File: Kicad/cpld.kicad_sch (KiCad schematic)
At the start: 16 parts, among them J2 Conn_01x06_Pin, U7 AMS1117-3.3, U9 XC95144XL-TQ144

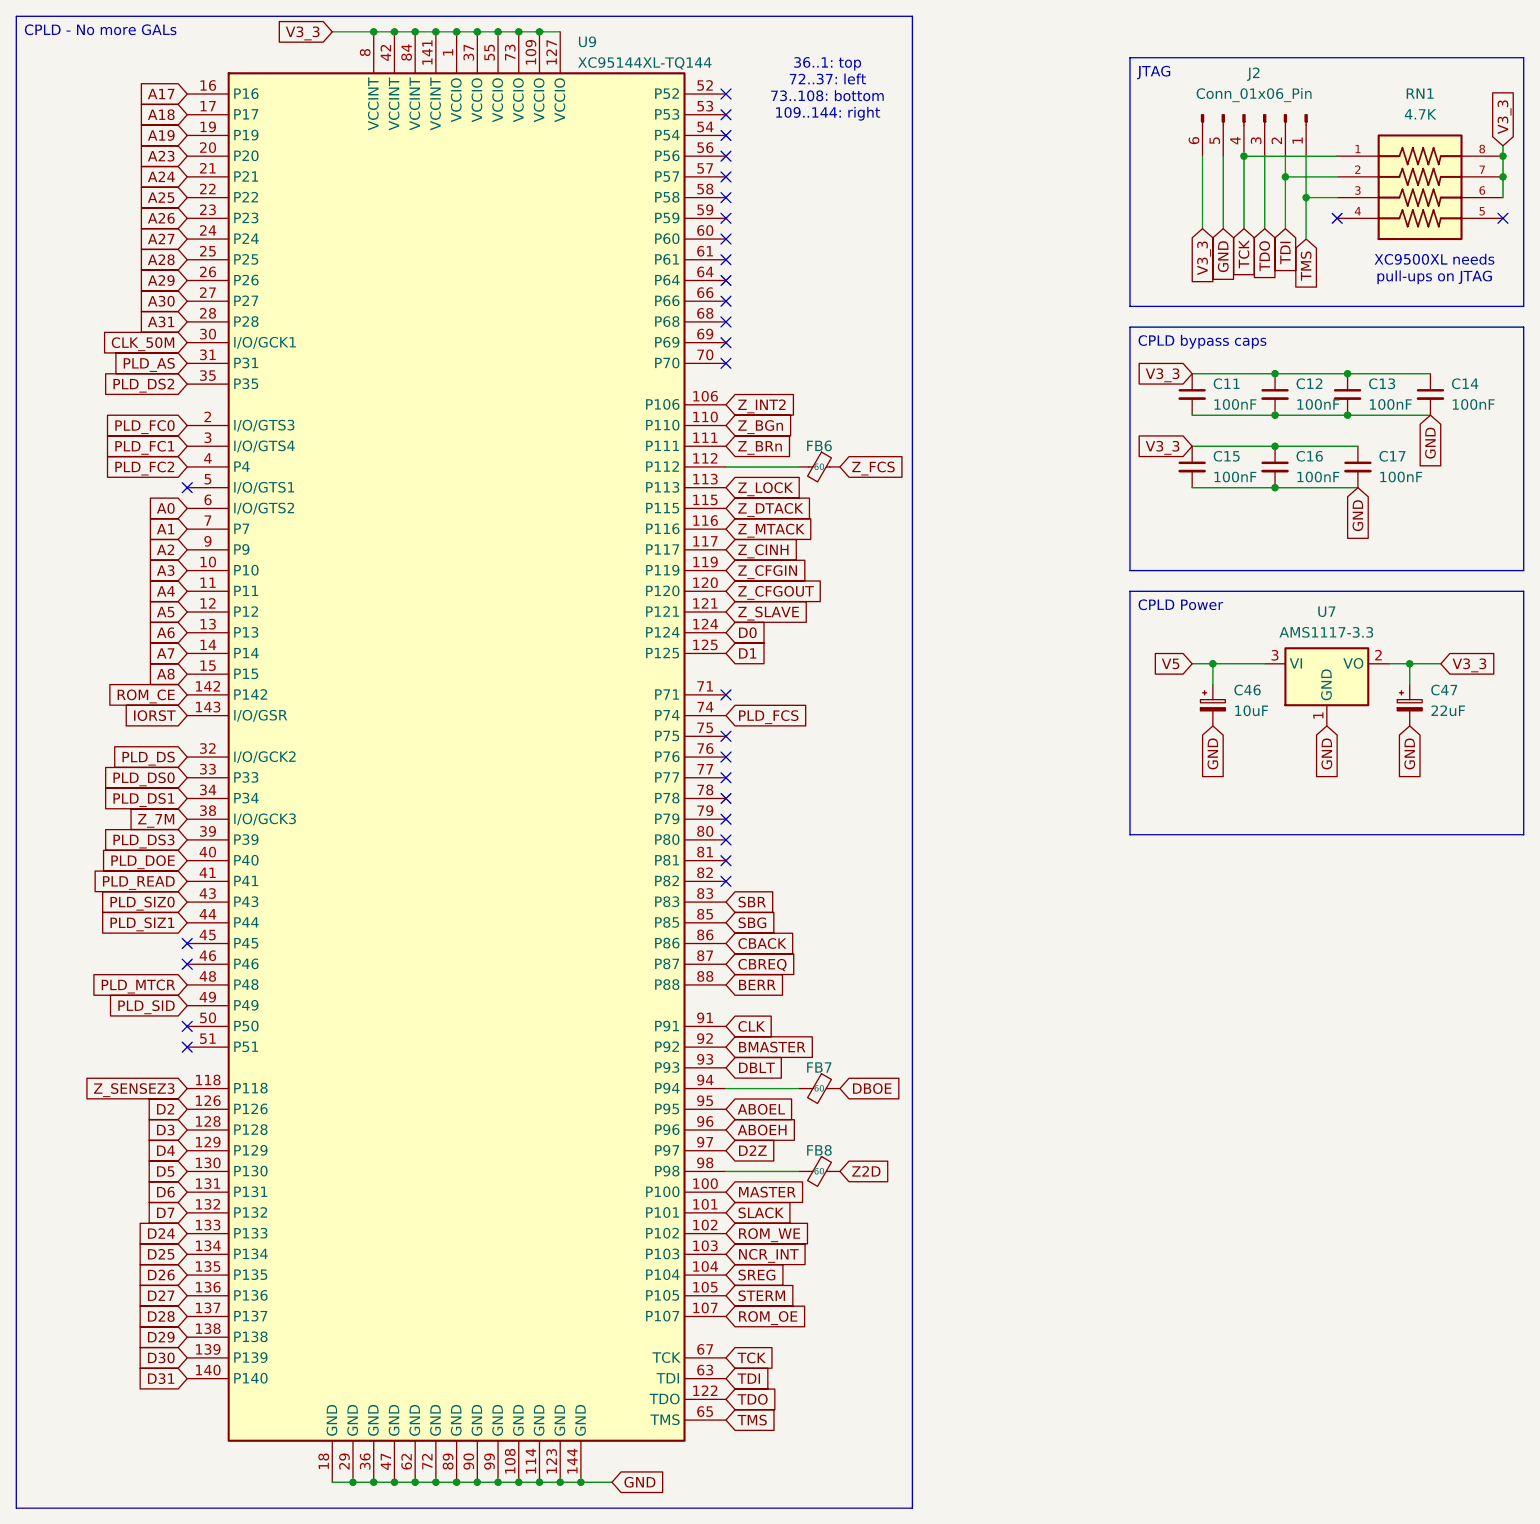
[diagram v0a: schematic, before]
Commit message: CPLD pin net swap (issue #7)
• PLD_FC0-FC2 nets move from Pin 2-4 to 75-77
• PLD_DS0-DS2 nets move from Pin 33-35 to 78-80
• ROM_WE net move from Pin 102  to 5
• ROM_OE net move from Pin 107 to 4

Additionally moved ROM_CE to P3 and PLD_DS3 to P81
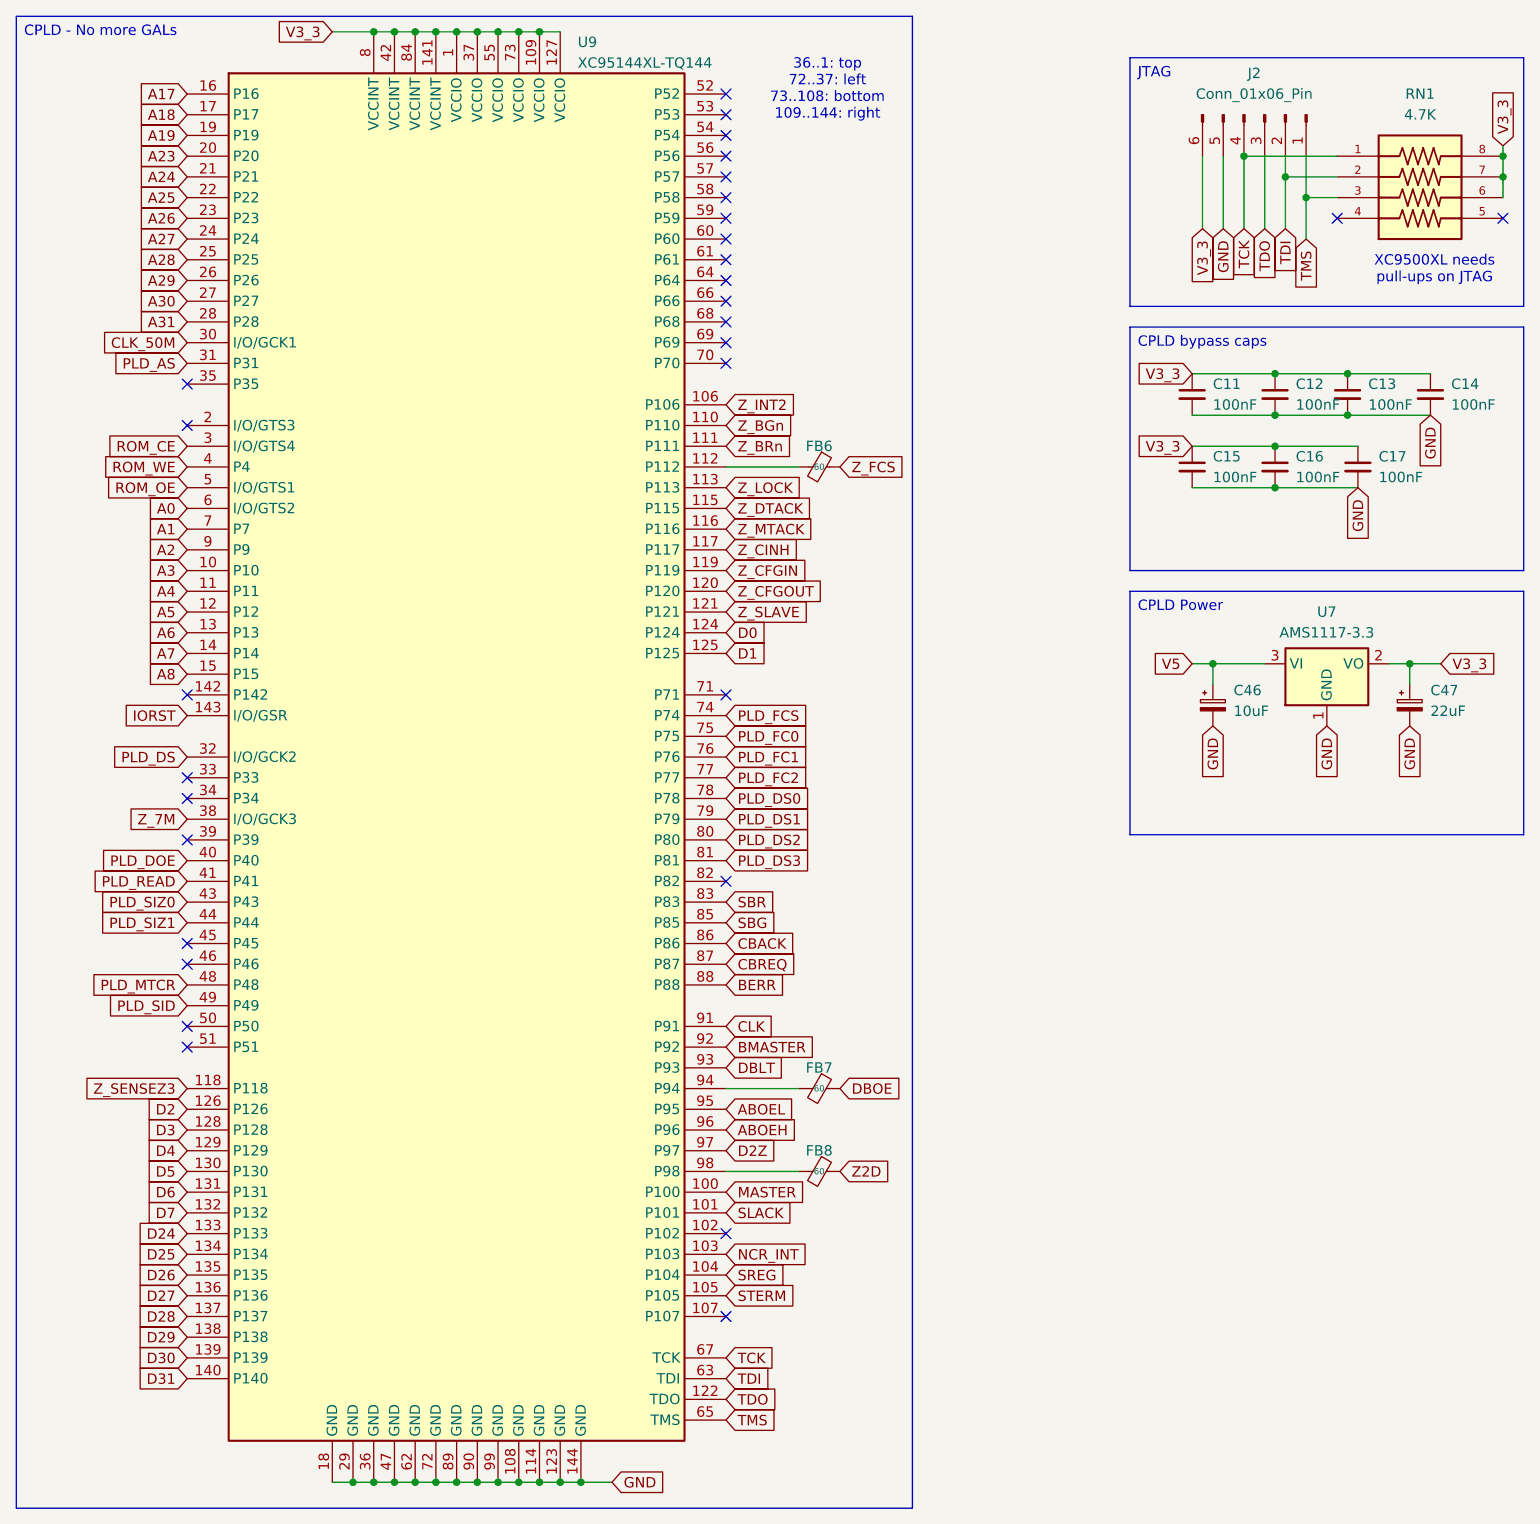
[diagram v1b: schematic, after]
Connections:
- net PLD_DS0: now also U9.78 (P78); no longer U9.33 (P33)
- net PLD_DS1: now also U9.79 (P79); no longer U9.34 (P34)
- net PLD_DS2: now also U9.80 (P80); no longer U9.35 (P35)
- net PLD_DS3: now also U9.81 (P81); no longer U9.39 (P39)
- net PLD_FC0: now also U9.75 (P75); no longer U9.2 (I/O/GTS3)
- net PLD_FC1: now also U9.76 (P76); no longer U9.3 (I/O/GTS4)
- net PLD_FC2: now also U9.77 (P77); no longer U9.4 (P4)
- net ROM_CE: now also U9.3 (I/O/GTS4); no longer U9.142 (P142)
- net ROM_OE: now also U9.5 (I/O/GTS1); no longer U9.107 (P107)
- net ROM_WE: now also U9.4 (P4); no longer U9.102 (P102)

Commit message: Update sheet, add pull down on ROM_CE
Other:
- company: (none) -> amiga.technology
- title: (none) -> A4092
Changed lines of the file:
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@@
 	(generator_version "9.0")
 	(paper "A4")
+	(title_block
+		(title "A4092")
+		(rev "PROTO0")
+		(company "amiga.technology")
+	)
 	(text "36..1: top\n72..37: left \n73..108: bottom\n109..144: right"
 		(exclude_from_sim no)

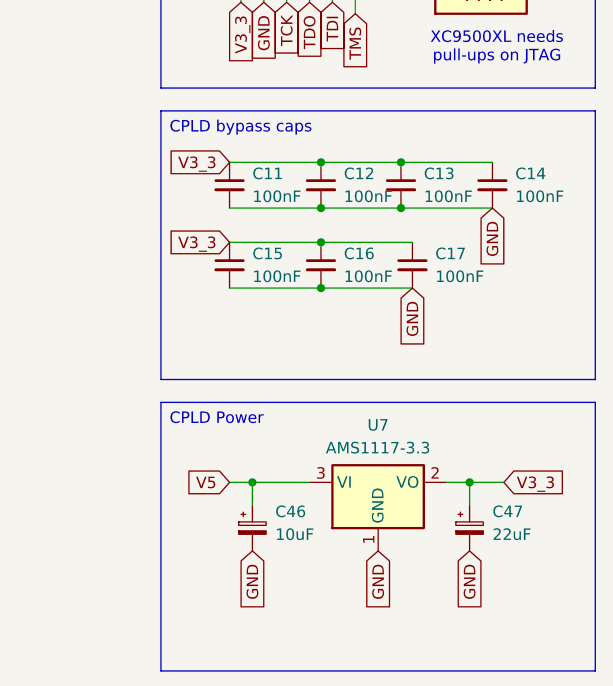
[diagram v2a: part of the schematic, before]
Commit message: Rename majority of bypass capacitors to match their Uxx
i.e. U4 will have C4A, C4B, C4C, C4D
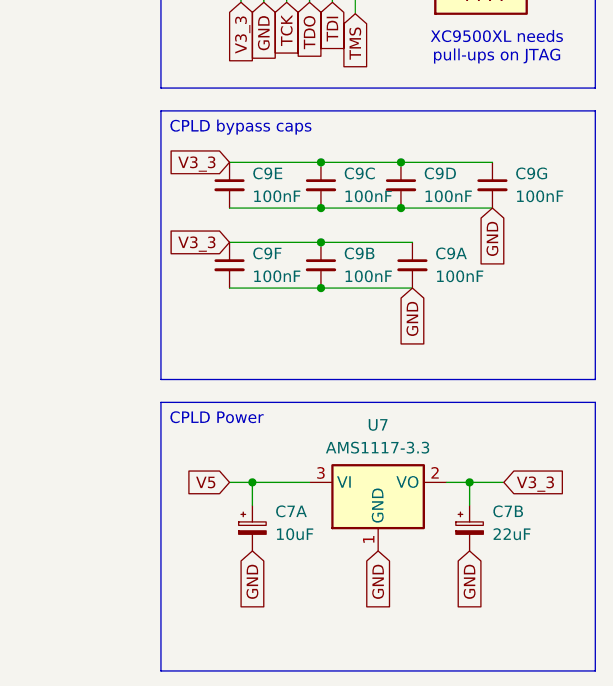
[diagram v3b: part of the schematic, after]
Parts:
- renumbered C46 to C7A, C47 to C7B, C17 to C9A, C16 to C9B, C12 to C9C, C13 to C9D, C11 to C9E, C15 to C9F, C14 to C9G
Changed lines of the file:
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@@
 		(dnp no)
 		(fields_autoplaced yes)
-		(property "Reference" "C15"
+		(property "Reference" "C9F"
 			(at 160.02 67.3162 0)
 			(effects
@@
 			(project "A4092"
 				(path "/8f9f4021-47aa-41d9-bea7-f6ccf72098bb/6ae4417c-9681-4757-b289-033d6e31deb3"
-					(reference "C15")
+					(reference "C9F")
 					(unit 1)
 				)
@@
 		(dnp no)
 		(fields_autoplaced yes)
-		(property "Reference" "C46"
+		(property "Reference" "C7A"
 			(at 162.56 95.9738 0)
 			(effects
@@
 			(project "A4092"
 				(path "/8f9f4021-47aa-41d9-bea7-f6ccf72098bb/6ae4417c-9681-4757-b289-033d6e31deb3"
-					(reference "C46")
+					(reference "C7A")
 					(unit 1)
 				)
@@
 		(dnp no)
 		(fields_autoplaced yes)
-		(property "Reference" "C17"
+		(property "Reference" "C9A"
 			(at 180.34 67.3162 0)
 			(effects
@@
 			(project "A4092"
 				(path "/8f9f4021-47aa-41d9-bea7-f6ccf72098bb/6ae4417c-9681-4757-b289-033d6e31deb3"
-					(reference "C17")
+					(reference "C9A")
 					(unit 1)
 				)
@@
 		(dnp no)
 		(fields_autoplaced yes)
-		(property "Reference" "C13"
+		(property "Reference" "C9D"
 			(at 179.07 58.4262 0)
 			(effects
@@
 			(project "A4092"
 				(path "/8f9f4021-47aa-41d9-bea7-f6ccf72098bb/6ae4417c-9681-4757-b289-033d6e31deb3"
-					(reference "C13")
+					(reference "C9D")
 					(unit 1)
 				)
@@
 		(dnp no)
 		(fields_autoplaced yes)
-		(property "Reference" "C11"
+		(property "Reference" "C9E"
 			(at 160.02 58.4262 0)
 			(effects
@@
 			(project ""
 				(path "/8f9f4021-47aa-41d9-bea7-f6ccf72098bb/6ae4417c-9681-4757-b289-033d6e31deb3"
-					(reference "C11")
+					(reference "C9E")
 					(unit 1)
 				)
@@
 		(dnp no)
 		(fields_autoplaced yes)
-		(property "Reference" "C14"
+		(property "Reference" "C9G"
 			(at 189.23 58.4262 0)
 			(effects
@@
 			(project "A4092"
 				(path "/8f9f4021-47aa-41d9-bea7-f6ccf72098bb/6ae4417c-9681-4757-b289-033d6e31deb3"
-					(reference "C14")
+					(reference "C9G")
 					(unit 1)
 				)
@@
 		(dnp no)
 		(fields_autoplaced yes)
-		(property "Reference" "C47"
+		(property "Reference" "C7B"
 			(at 186.69 95.9738 0)
 			(effects
@@
 			(project "A4092"
 				(path "/8f9f4021-47aa-41d9-bea7-f6ccf72098bb/6ae4417c-9681-4757-b289-033d6e31deb3"
-					(reference "C47")
+					(reference "C7B")
 					(unit 1)
 				)
@@
 		(dnp no)
 		(fields_autoplaced yes)
-		(property "Reference" "C12"
+		(property "Reference" "C9C"
 			(at 170.18 58.4262 0)
 			(effects
@@
 			(project ""
 				(path "/8f9f4021-47aa-41d9-bea7-f6ccf72098bb/6ae4417c-9681-4757-b289-033d6e31deb3"
-					(reference "C12")
+					(reference "C9C")
 					(unit 1)
 				)
@@
 		(dnp no)
 		(fields_autoplaced yes)
-		(property "Reference" "C16"
+		(property "Reference" "C9B"
 			(at 170.18 67.3162 0)
 			(effects
@@
 			(project "A4092"
 				(path "/8f9f4021-47aa-41d9-bea7-f6ccf72098bb/6ae4417c-9681-4757-b289-033d6e31deb3"
-					(reference "C16")
-					(unit 1)
-				)
+					(reference "C9B")
+					(unit 1)
+				)

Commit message: Revert: Rename majority of bypass capacitors to match their Uxx
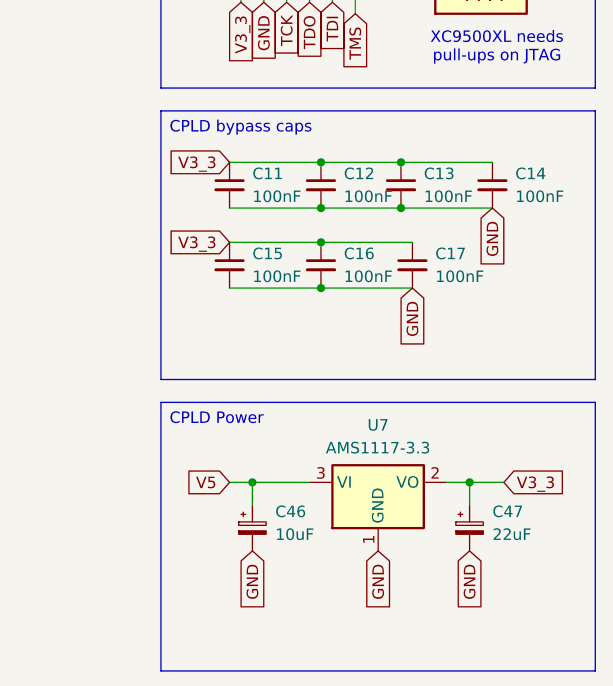
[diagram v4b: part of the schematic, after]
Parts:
- renumbered C9E to C11, C9C to C12, C9D to C13, C9G to C14, C9F to C15, C9B to C16, C9A to C17, C7A to C46, C7B to C47
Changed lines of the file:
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@@
 		(dnp no)
 		(fields_autoplaced yes)
-		(property "Reference" "C9F"
+		(property "Reference" "C15"
 			(at 160.02 67.3162 0)
 			(effects
@@
 			(project "A4092"
 				(path "/8f9f4021-47aa-41d9-bea7-f6ccf72098bb/6ae4417c-9681-4757-b289-033d6e31deb3"
-					(reference "C9F")
+					(reference "C15")
 					(unit 1)
 				)
@@
 		(dnp no)
 		(fields_autoplaced yes)
-		(property "Reference" "C7A"
+		(property "Reference" "C46"
 			(at 162.56 95.9738 0)
 			(effects
@@
 			(project "A4092"
 				(path "/8f9f4021-47aa-41d9-bea7-f6ccf72098bb/6ae4417c-9681-4757-b289-033d6e31deb3"
-					(reference "C7A")
+					(reference "C46")
 					(unit 1)
 				)
@@
 		(dnp no)
 		(fields_autoplaced yes)
-		(property "Reference" "C9A"
+		(property "Reference" "C17"
 			(at 180.34 67.3162 0)
 			(effects
@@
 			(project "A4092"
 				(path "/8f9f4021-47aa-41d9-bea7-f6ccf72098bb/6ae4417c-9681-4757-b289-033d6e31deb3"
-					(reference "C9A")
+					(reference "C17")
 					(unit 1)
 				)
@@
 		(dnp no)
 		(fields_autoplaced yes)
-		(property "Reference" "C9D"
+		(property "Reference" "C13"
 			(at 179.07 58.4262 0)
 			(effects
@@
 			(project "A4092"
 				(path "/8f9f4021-47aa-41d9-bea7-f6ccf72098bb/6ae4417c-9681-4757-b289-033d6e31deb3"
-					(reference "C9D")
+					(reference "C13")
 					(unit 1)
 				)
@@
 		(dnp no)
 		(fields_autoplaced yes)
-		(property "Reference" "C9E"
+		(property "Reference" "C11"
 			(at 160.02 58.4262 0)
 			(effects
@@
 			(project ""
 				(path "/8f9f4021-47aa-41d9-bea7-f6ccf72098bb/6ae4417c-9681-4757-b289-033d6e31deb3"
-					(reference "C9E")
+					(reference "C11")
 					(unit 1)
 				)
@@
 		(dnp no)
 		(fields_autoplaced yes)
-		(property "Reference" "C9G"
+		(property "Reference" "C14"
 			(at 189.23 58.4262 0)
 			(effects
@@
 			(project "A4092"
 				(path "/8f9f4021-47aa-41d9-bea7-f6ccf72098bb/6ae4417c-9681-4757-b289-033d6e31deb3"
-					(reference "C9G")
+					(reference "C14")
 					(unit 1)
 				)
@@
 		(dnp no)
 		(fields_autoplaced yes)
-		(property "Reference" "C7B"
+		(property "Reference" "C47"
 			(at 186.69 95.9738 0)
 			(effects
@@
 			(project "A4092"
 				(path "/8f9f4021-47aa-41d9-bea7-f6ccf72098bb/6ae4417c-9681-4757-b289-033d6e31deb3"
-					(reference "C7B")
+					(reference "C47")
 					(unit 1)
 				)
@@
 		(dnp no)
 		(fields_autoplaced yes)
-		(property "Reference" "C9C"
+		(property "Reference" "C12"
 			(at 170.18 58.4262 0)
 			(effects
@@
 			(project ""
 				(path "/8f9f4021-47aa-41d9-bea7-f6ccf72098bb/6ae4417c-9681-4757-b289-033d6e31deb3"
-					(reference "C9C")
+					(reference "C12")
 					(unit 1)
 				)
@@
 		(dnp no)
 		(fields_autoplaced yes)
-		(property "Reference" "C9B"
+		(property "Reference" "C16"
 			(at 170.18 67.3162 0)
 			(effects
@@
 			(project "A4092"
 				(path "/8f9f4021-47aa-41d9-bea7-f6ccf72098bb/6ae4417c-9681-4757-b289-033d6e31deb3"
-					(reference "C9B")
-					(unit 1)
-				)
+					(reference "C16")
+					(unit 1)
+				)

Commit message: Replace C47 and C46 with Tantalum capacitors
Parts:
- C46, C47: footprint Capacitor_SMD:CP_Elec_6.3x7.7 -> Capacitor_Tantalum_SMD:CP_EIA-3528-15_AVX-H_HandSolder
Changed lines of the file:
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@@
 			)
 		)
-		(property "Footprint" "Capacitor_SMD:CP_Elec_6.3x7.7"
+		(property "Footprint" "Capacitor_Tantalum_SMD:CP_EIA-3528-15_AVX-H_HandSolder"
 			(at 160.02 97.79 0)
 			(effects
@@
 			)
 		)
-		(property "Footprint" "Capacitor_SMD:CP_Elec_6.3x7.7"
+		(property "Footprint" "Capacitor_Tantalum_SMD:CP_EIA-3528-15_AVX-H_HandSolder"
 			(at 184.15 97.79 0)
 			(effects
